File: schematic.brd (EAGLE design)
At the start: 100 x 80 mm, 32 parts, among them Q1 FDN360P, Q3 BSS123

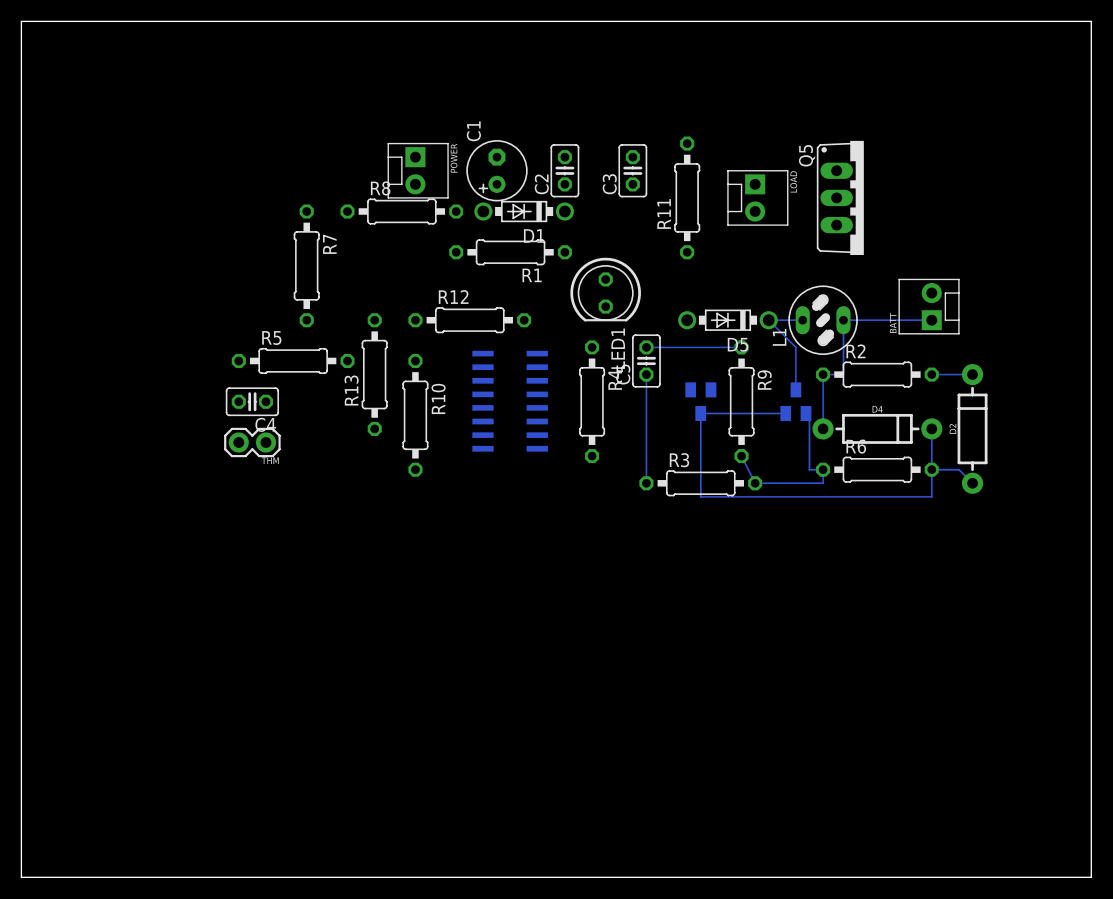
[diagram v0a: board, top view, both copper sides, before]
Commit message: Improved routing
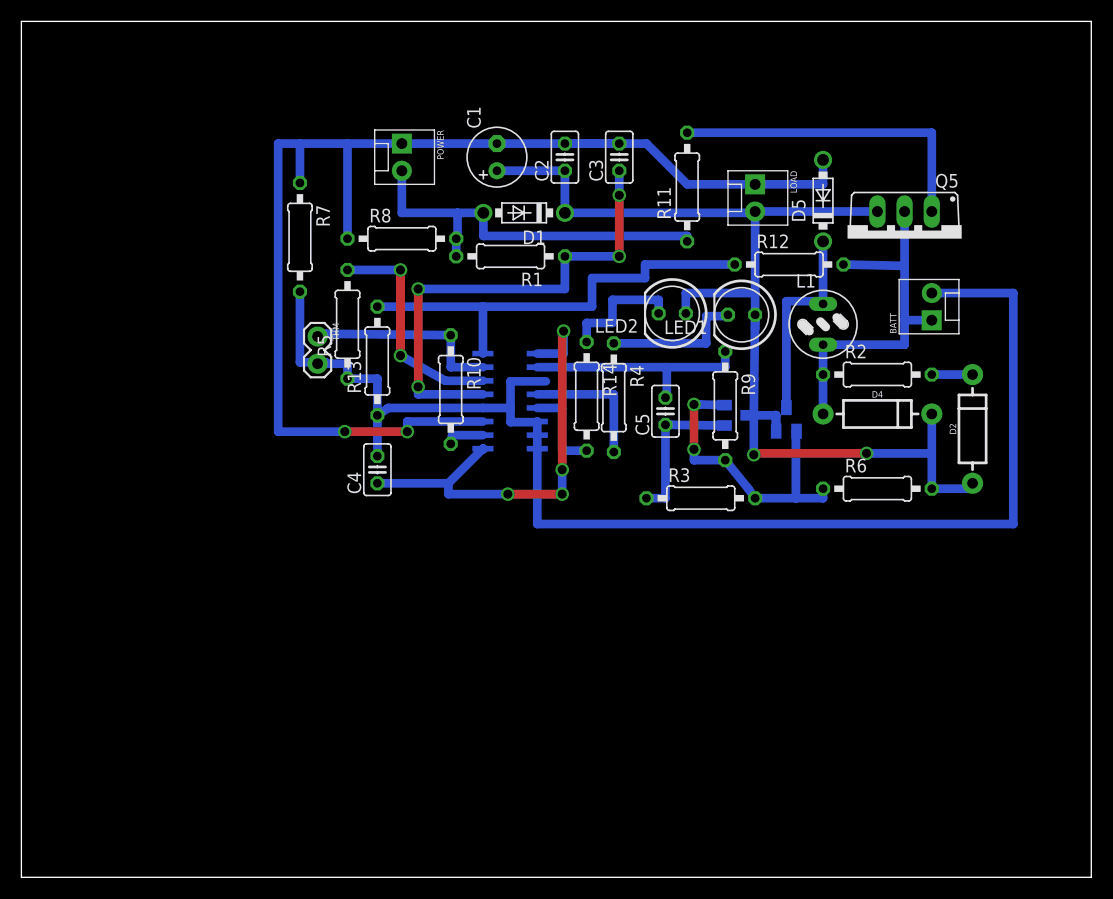
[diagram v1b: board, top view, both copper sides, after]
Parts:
- added LED2: (no value), led:LED5MM
- added R14: 1k, rcl:0207/10
- moved R12 30.3 mm to (71.8, 57.3)
- moved D5 14.3 mm to (74.9, 63.2), turned to 90 degrees
- moved C4 13.3 mm to (33.3, 38.1), turned to 90 degrees
- moved LED1 12.9 mm to (67.3, 52.6), turned to 180 degrees
- moved THM 11.0 mm to (27.7, 50.5), turned to 270 degrees
- moved R5 6.13 mm to (30.5, 51.7), turned to 90 degrees
- moved Q5 5.39 mm to (82.5, 59.7), turned to 180 degrees
- moved C5 5.02 mm to (60.2, 43.6)
- moved R10 4.09 mm to (40.1, 45.6)
- moved Q3 3.54 mm to (66.8, 43.2), turned to 90 degrees
- moved R7 2.74 mm to (26.0, 59.8)
- moved R8 2.54 mm to (35.6, 59.7)
- moved R4 2.07 mm to (55.4, 44.8)
- moved Q1 1.88 mm to (71.5, 42.8)
- moved C3 1.80 mm to (55.9, 67.3)
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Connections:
- new net N$2: LED2.K, R14.1
- new net N$3: R14.2, U$1.5
- net N$26: now also LED2.A
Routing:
- net N$4: track 0.00 -> 129.6 mm
- net GND: track 0.00 -> 119.4 mm, vias 0 -> 2
- net N$26: track 48.0 -> 106.0 mm, vias 0 -> 2
- net N$19: track 0.00 -> 45.8 mm, vias 0 -> 4
- net N$23: track 0.00 -> 43.0 mm, vias 0 -> 4
- net N$7: track 0.00 -> 41.7 mm
- net N$25: track 0.00 -> 37.5 mm
- net N$1: track 0.00 -> 30.2 mm
- net N$20: track 0.00 -> 21.3 mm, vias 0 -> 2
- net N$5: track 0.00 -> 18.5 mm
- net N$8: track 20.3 -> 34.8 mm
- net N$15: track 0.00 -> 13.3 mm
- net N$12: track 8.89 -> 22.0 mm
- net N$9: track 0.00 -> 12.5 mm
- net N$2: track 0.00 -> 11.9 mm
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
